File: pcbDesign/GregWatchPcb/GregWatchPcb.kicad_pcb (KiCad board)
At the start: 2 copper layers, 37 parts, among them J1 AVR-ISP-6, SW1 SW_Push, SW2 SW_Push, SW3 SW_Push, SW4 SW_Push, U1 Nokia_5110_LCD, U2 ATmega328P-AU, U3 74HC14, Y1 16M

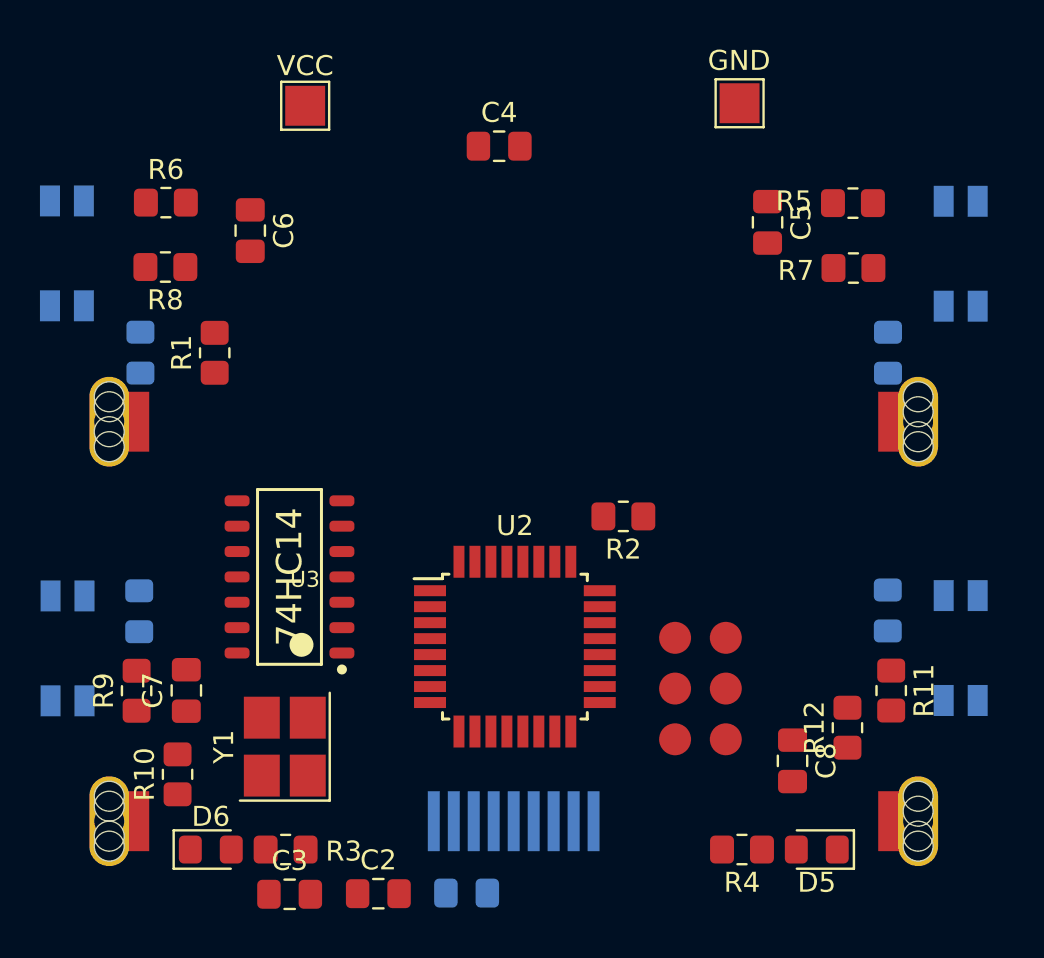
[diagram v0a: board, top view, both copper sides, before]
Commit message: Added connection for all components on the board
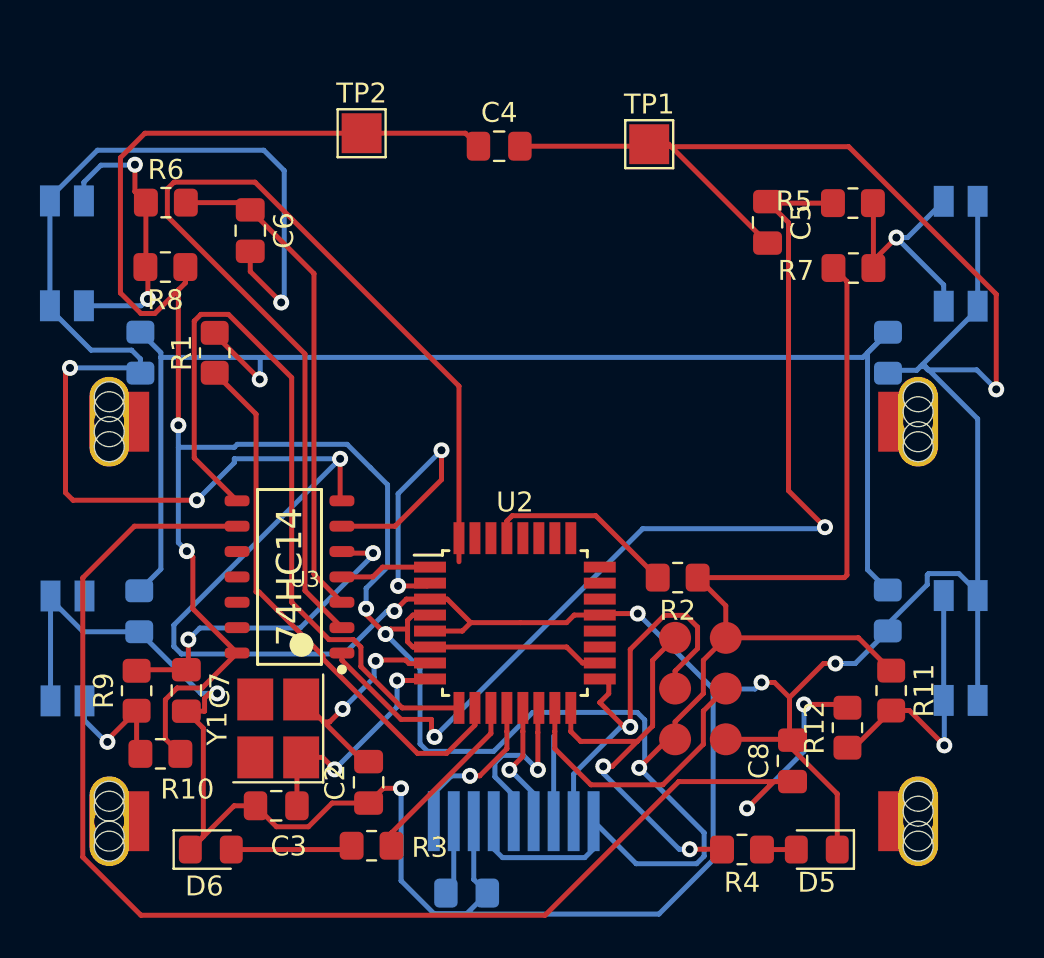
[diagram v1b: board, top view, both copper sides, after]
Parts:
- removed GND, VCC: TestPoint_Pad_2.0x2.0mm, TestPoint:TestPoint_Pad_2.0x2.0mm
- added TP1: TestPoint, TestPoint:TestPoint_Pad_2.0x2.0mm, F.Cu at (144.9, 28.6)
- added TP2: TestPoint, TestPoint:TestPoint_Pad_2.0x2.0mm, F.Cu at (130.5, 28.1)
- moved C2 5.60 mm to (130.8, 60.6), turned to 90 degrees
- moved C3 4.48 mm to (126.2, 61.8)
- moved R3 4.31 mm to (131.0, 63.8)
- moved R2 4.10 mm to (146.3, 50.3)
- moved R10 1.34 mm to (120.4, 59.1), turned to 180 degrees
- moved U2 1.18 mm to (138.2, 52.6)
- moved Y1 0.97 mm to (126.3, 57.9)
- turned C7 to 270 degrees
- turned C8 to 90 degrees
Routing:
- net GND: track 0.00 -> 284.8 mm, vias 0 -> 11
- net +5V: track 0.00 -> 176.7 mm, vias 0 -> 5
- net Net-(C8-Pad1): track 0.00 -> 73.7 mm, vias 0 -> 2
- net Net-(D1-Pad2): track 0.00 -> 68.9 mm, vias 0 -> 1
- net Net-(U2-Pad32): track 0.00 -> 53.4 mm
- net Net-(C5-Pad1): track 0.00 -> 51.7 mm, vias 0 -> 2
- net Net-(U2-Pad9): track 0.00 -> 38.6 mm
- net Net-(R1-Pad1): track 0.00 -> 27.7 mm
- net Net-(C6-Pad1): track 0.00 -> 24.9 mm
- net Net-(J1-Pad3): track 0.00 -> 21.7 mm, vias 0 -> 1
- net Net-(J1-Pad1): track 0.00 -> 21.0 mm, vias 0 -> 2
- net Net-(J1-Pad4): track 0.00 -> 18.6 mm
- net Net-(U2-Pad2): track 0.00 -> 16.8 mm, vias 0 -> 2
- net Net-(C7-Pad1): track 0.00 -> 16.8 mm, vias 0 -> 2
- net Net-(R6-Pad1): track 0.00 -> 14.2 mm, vias 0 -> 2
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
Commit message: Add battery to schematic and JST connector for the battery to the PCB
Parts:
- added BT1: Battery_Cell, Connector_JST:JST_EH_S2B-EH_1x02_P2.50mm_Horizontal, F.Cu at (147.3, 97.8)
- moved R6 56.2 mm to (127.0, 87.4)
- moved U1 56.2 mm to (144.4, 120.9)
- moved C4 56.2 mm to (143.7, 84.6)
- moved C5 56.2 mm to (157.2, 88.4)
- moved C7 56.2 mm to (128.1, 111.9)
- moved D4 56.2 mm to (125.7, 107.9)
- moved R1 56.2 mm to (129.5, 95.0)
- moved R10 56.2 mm to (126.8, 115.0)
- moved R11 56.2 mm to (163.3, 111.9)
- moved R8 56.2 mm to (127.0, 90.7)
- moved R9 56.2 mm to (125.6, 111.9)
- moved SW3 56.2 mm to (122.1, 109.8)
- moved SW4 56.2 mm to (166.8, 109.7)
- moved U2 56.2 mm to (144.5, 108.5)
- moved U3 56.2 mm to (133.2, 106.2)
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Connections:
- net +5V renamed Net-(BT1-Pad1)
- net GND renamed Net-(BT1-Pad2)
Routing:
- net Net-(BT1-Pad2): track 284.8 -> 300.1 mm
- net Net-(BT1-Pad1): track 176.7 -> 191.8 mm
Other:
- board outline added: 50.8 x 43.2 mm
